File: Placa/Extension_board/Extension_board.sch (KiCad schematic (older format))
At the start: 4 parts

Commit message: Finalizacion del esquematico y creacion del layout
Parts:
- removed C?: C, symbol Device:C
- added D1: D_Zener, Diode_SMD:D_0805_2012Metric, symbol Device:D_Zener
- added D2, D3: LED, Diode_SMD:D_0805_2012Metric, symbol Device:LED
- added J3: Conn_01x04_Male, Connector_PinHeader_1.27mm:PinHeader_1x04_P1.27mm_Vertical, symbol Connector:Conn_01x04_Male
- added R1, R2, R3: 1Ω, Resistor_SMD:R_0805_2012Metric, symbol Device:R
- added R4, R5: 1kΩ, Resistor_SMD:R_0805_2012Metric, symbol Device:R
- J1: renamed from J?; footprint (none) -> Connector_PinHeader_1.27mm:PinHeader_1x05_P1.27mm_Vertical
- J2: renamed from J?; footprint (none) -> Connector_USB:USB_Micro-B_Wuerth_629105150521
- U1: renamed from U?; footprint XDCR_STEVAL-STLCS01V1 -> STEVAL-STLCS01V1_footprint:XDCR_STEVAL-STLCS01V1
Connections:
- net labels added: VIN
- net labels removed: 3.3V, MIC_CLK, SD_CS, SD_MISO, SD_MOSI, SD_SCK
- wire segments 16 -> 24
- no-connect marks 2 -> 10
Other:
- note added: "N3-I2C"
- note added: "N4-Regulación"
- note added: "N5-LEDs"
- note added: "N6-STEVAL-STLCR01V1"
- note added: "Rpz=(Vs-Vz)/((Iz*1.1)+Il)\nRpz=(5v-4.7v)/(53mA*1.1+100mA)\nRpz=2,84Ω"
- note removed: "Dudas:\nD1: La disposicion de los pines del simbolo Micro USB,\n no son identicas al estipulado en el pdf del fabricante, \npor ende se opto por usar estas ultimas disposiciones. \nComprobar si son correctas."
- note removed: "N3-STEVAL-STLCR01V1"
- moved on the sheet: J2, U1

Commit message: Version 2.1 del proyecto
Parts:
- removed D3: LED, Diode_SMD:D_0805_2012Metric, symbol Device:LED
- removed J1: Conn_01x05_Male, Connector_PinHeader_1.27mm:PinHeader_1x05_P1.27mm_Vertical, symbol Connector:Conn_01x05_Male
- removed R2, R3: 1Ω, Resistor_SMD:R_0805_2012Metric, symbol Device:R
- removed R5: 1kΩ, Resistor_SMD:R_0805_2012Metric, symbol Device:R
- added J1: USB_B_Micro, Connector_USB:USB_Micro-B_Wuerth_629105150521, symbol Connector:USB_B_Micro
- J3: footprint Connector_PinHeader_1.27mm:PinHeader_1x04_P1.27mm_Vertical -> Connector_PinHeader_1.00mm:PinHeader_1x04_P1.00mm_Vertical_SMD_Pin1Left
- R1: value 1Ω -> 1,2Ω
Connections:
- net GND: now also J1.5 (GND)
- net RESET: now also J1.3 (D+)
- net SWDCLK: now also J1.2 (D-)
- net SWDIO: now also J1.1 (VBUS)
- net VIN: now also J3.1 (Pin_1), R1.1
- net V_USB: no longer J3.1 (Pin_1)
- no-connect marks 10 -> 11
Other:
- note added: "Rpz=(Vs-Vz)/((Iz*1.1)+Il+Ii2c)\nRpz=(5v-3.3v)/(53mA*1.1+100mA+150mA)\nRpz=1.2Ω"
- note removed: "Rpz=(Vs-Vz)/((Iz*1.1)+Il)\nRpz=(5v-4.7v)/(53mA*1.1+100mA)\nRpz=2,84Ω"
- moved on the sheet: D1, D2, R1, R4
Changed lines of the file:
@@
 Text Notes 1000 1050 0    50   ~ 0
 N1-Entrada_de_voltaje
-$Comp
-L Connector:Conn_01x05_Male J1
-U 1 1 60BBD811
-P 1350 3100
-F 0 "J1" H 1458 3481 50  0000 C CNN
-F 1 "Conn_01x05_Male" H 1458 3390 50  0000 C CNN
-F 2 "Connector_PinHeader_1.27mm:PinHeader_1x05_P1.27mm_Vertical" H 1350 3100 50  0001 C CNN
-F 3 "~" H 1350 3100 50  0001 C CNN
-	1    1350 3100
-	1    0    0    -1
-$EndComp
-Wire Wire Line
-	1550 3000 1850 3000
-Wire Wire Line
-	1550 3100 1850 3100
-Wire Wire Line
-	1550 3200 1850 3200
-Wire Wire Line
-	1550 3300 1850 3300
-Wire Wire Line
-	1550 2900 1850 2900
-NoConn ~ 1850 2900
-Text Label 1850 3000 0    50   ~ 0
+Text Label 1800 3300 0    50   ~ 0
 SWDCLK
-Text Label 1850 3100 0    50   ~ 0
-GND
-Text Label 1850 3200 0    50   ~ 0
+Text Label 1800 3400 0    50   ~ 0
+GND
+Text Label 1800 3100 0    50   ~ 0
 SWDIO
-Text Label 1850 3300 0    50   ~ 0
+Text Label 1800 3200 0    50   ~ 0
 RESET
-Wire Notes Line
-	1000 2650 1000 3500
-Wire Notes Line
-	1000 3500 2200 3500
-Wire Notes Line
-	2200 3500 2200 2650
 Wire Notes Line
 	2200 2650 1000 2650
@@
 L Device:D_Zener D1
 U 1 1 60BFFB26
-P 2450 4400
-F 0 "D1" V 2404 4480 50  0000 L CNN
-F 1 "D_Zener" V 2495 4480 50  0000 L CNN
-F 2 "Diode_SMD:D_0805_2012Metric" H 2450 4400 50  0001 C CNN
-F 3 "~" H 2450 4400 50  0001 C CNN
-	1    2450 4400
+P 2400 4650
+F 0 "D1" V 2354 4730 50  0000 L CNN
+F 1 "D_Zener" V 2445 4730 50  0000 L CNN
+F 2 "Diode_SMD:D_0805_2012Metric" H 2400 4650 50  0001 C CNN
+F 3 "~" H 2400 4650 50  0001 C CNN
+	1    2400 4650
 	0    1    1    0
 $EndComp
-Text Label 1250 4050 2    50   ~ 0
+Text Label 1200 4300 2    50   ~ 0
 V_USB
-Text Label 1200 4550 2    50   ~ 0
-GND
-Text Label 2600 4050 0    50   ~ 0
+Text Label 1150 4800 2    50   ~ 0
+GND
+Text Label 2550 4300 0    50   ~ 0
 VIN
 $Comp
 L Device:R R1
 U 1 1 60C00A3D
-P 1400 4050
-F 0 "R1" V 1193 4050 50  0000 C CNN
-F 1 "1Ω" V 1284 4050 50  0000 C CNN
-F 2 "Resistor_SMD:R_0805_2012Metric" V 1330 4050 50  0001 C CNN
-F 3 "~" H 1400 4050 50  0001 C CNN
-	1    1400 4050
+P 1850 4300
+F 0 "R1" V 1643 4300 50  0000 C CNN
+F 1 "1,2Ω" V 1734 4300 50  0000 C CNN
+F 2 "Resistor_SMD:R_0805_2012Metric" V 1780 4300 50  0001 C CNN
+F 3 "~" H 1850 4300 50  0001 C CNN
+	1    1850 4300
 	0    1    1    0
 $EndComp
-Text Notes 1000 3700 0    50   ~ 0
+Text Notes 950  3950 0    50   ~ 0
 N4-Regulación
 NoConn ~ 4250 2250
@@
 Text Notes 2350 2600 0    50   ~ 0
 N3-I2C
-$Comp
-L Device:R R2
-U 1 1 60C21078
-P 1800 4050
-F 0 "R2" V 2007 4050 50  0000 C CNN
-F 1 "1Ω" V 1916 4050 50  0000 C CNN
-F 2 "Resistor_SMD:R_0805_2012Metric" V 1730 4050 50  0001 C CNN
-F 3 "~" H 1800 4050 50  0001 C CNN
-	1    1800 4050
-	0    -1   -1   0
-$EndComp
-$Comp
-L Device:R R3
-U 1 1 60C2144B
-P 2200 4050
-F 0 "R3" V 2407 4050 50  0000 C CNN
-F 1 "1Ω" V 2316 4050 50  0000 C CNN
-F 2 "Resistor_SMD:R_0805_2012Metric" V 2130 4050 50  0001 C CNN
-F 3 "~" H 2200 4050 50  0001 C CNN
-	1    2200 4050
-	0    -1   -1   0
-$EndComp
-Wire Wire Line
-	1550 4050 1650 4050
-Wire Wire Line
-	1950 4050 2050 4050
-Wire Wire Line
-	1200 4550 2450 4550
-Wire Wire Line
-	2450 4250 2450 4050
-Wire Wire Line
-	2450 4050 2350 4050
-Wire Wire Line
-	2450 4050 2600 4050
-Connection ~ 2450 4050
-Wire Notes Line
-	1000 3750 1000 4600
-Wire Notes Line
-	1000 4600 2850 4600
-Wire Notes Line
-	2850 4600 2850 3750
-Wire Notes Line
-	1000 3750 2850 3750
-Text Label 3100 2900 0    50   ~ 0
-V_USB
+Wire Wire Line
+	1150 4800 2400 4800
+Wire Wire Line
+	2400 4500 2400 4300
+Wire Wire Line
+	2400 4300 2550 4300
+Wire Notes Line
+	950  4000 950  4850
+Wire Notes Line
+	950  4850 2800 4850
+Wire Notes Line
+	2800 4850 2800 4000
+Wire Notes Line
+	950  4000 2800 4000
 Text Label 3100 3200 0    50   ~ 0
 GND
@@
 F 0 "J3" H 2708 3281 50  0000 C CNN
 F 1 "Conn_01x04_Male" H 2708 3190 50  0000 C CNN
-F 2 "Connector_PinHeader_1.27mm:PinHeader_1x04_P1.27mm_Vertical" H 2600 3000 50  0001 C CNN
+F 2 "Connector_PinHeader_1.00mm:PinHeader_1x04_P1.00mm_Vertical_SMD_Pin1Left" H 2600 3000 50  0001 C CNN
 F 3 "~" H 2600 3000 50  0001 C CNN
 	1    2600 3000
@@
 Wire Wire Line
 	1650 2200 2300 2200
-Text Notes 3000 4300 0    59   ~ 0
-Rpz=(Vs-Vz)/((Iz*1.1)+Il)\nRpz=(5v-4.7v)/(53mA*1.1+100mA)\nRpz=2,84Ω
+Text Notes 2950 4550 0    59   ~ 0
+Rpz=(Vs-Vz)/((Iz*1.1)+Il+Ii2c)\nRpz=(5v-3.3v)/(53mA*1.1+100mA+150mA)\nRpz=1.2Ω
 $Comp
 L Device:LED D2
 U 1 1 60C6CD3B
-P 2050 5150
-F 0 "D2" H 2043 4895 50  0000 C CNN
-F 1 "LED" H 2043 4986 50  0000 C CNN
-F 2 "Diode_SMD:D_0805_2012Metric" H 2050 5150 50  0001 C CNN
-F 3 "~" H 2050 5150 50  0001 C CNN
-	1    2050 5150
-	-1   0    0    1
-$EndComp
-$Comp
-L Device:LED D3
-U 1 1 60C6DA9C
-P 2050 5500
-F 0 "D3" H 2043 5245 50  0000 C CNN
-F 1 "LED" H 2043 5336 50  0000 C CNN
-F 2 "Diode_SMD:D_0805_2012Metric" H 2050 5500 50  0001 C CNN
-F 3 "~" H 2050 5500 50  0001 C CNN
-	1    2050 5500
+P 2000 5400
+F 0 "D2" H 1993 5145 50  0000 C CNN
+F 1 "LED" H 1993 5236 50  0000 C CNN
+F 2 "Diode_SMD:D_0805_2012Metric" H 2000 5400 50  0001 C CNN
+F 3 "~" H 2000 5400 50  0001 C CNN
+	1    2000 5400
 	-1   0    0    1
 $EndComp
@@
 L Device:R R4
 U 1 1 60C6E1B1
-P 1500 5150
-F 0 "R4" V 1293 5150 50  0000 C CNN
-F 1 "1kΩ" V 1384 5150 50  0000 C CNN
-F 2 "Resistor_SMD:R_0805_2012Metric" V 1430 5150 50  0001 C CNN
-F 3 "~" H 1500 5150 50  0001 C CNN
-	1    1500 5150
+P 1450 5400
+F 0 "R4" V 1243 5400 50  0000 C CNN
+F 1 "1kΩ" V 1334 5400 50  0000 C CNN
+F 2 "Resistor_SMD:R_0805_2012Metric" V 1380 5400 50  0001 C CNN
+F 3 "~" H 1450 5400 50  0001 C CNN
+	1    1450 5400
 	0    1    1    0
 $EndComp
-$Comp
-L Device:R R5
-U 1 1 60C6E5D7
-P 1500 5500
-F 0 "R5" V 1293 5500 50  0000 C CNN
-F 1 "1kΩ" V 1384 5500 50  0000 C CNN
-F 2 "Resistor_SMD:R_0805_2012Metric" V 1430 5500 50  0001 C CNN
-F 3 "~" H 1500 5500 50  0001 C CNN
-	1    1500 5500
-	0    1    1    0
-$EndComp
-Text Label 2450 5150 0    50   ~ 0
-GND
-Text Label 2450 5500 0    50   ~ 0
-GND
-Wire Wire Line
-	2200 5500 2450 5500
-Wire Wire Line
-	2200 5150 2450 5150
-Wire Wire Line
-	1650 5150 1900 5150
-Wire Wire Line
-	1650 5500 1900 5500
-Text Label 1350 5150 2    50   ~ 0
+Text Label 2400 5400 0    50   ~ 0
+GND
+Wire Wire Line
+	2150 5400 2400 5400
+Wire Wire Line
+	1600 5400 1850 5400
+Text Label 1300 5400 2    50   ~ 0
 V_USB
-Text Label 1350 5500 2    50   ~ 0
-SWDCLK
-Wire Notes Line
-	1000 4850 1000 5600
-Wire Notes Line
-	1000 5600 2650 5600
-Wire Notes Line
-	2650 5600 2650 4850
-Wire Notes Line
-	2650 4850 1000 4850
-Text Notes 1050 4800 0    50   ~ 0
+Wire Notes Line
+	2600 5100 950  5100
+Text Notes 1000 5050 0    50   ~ 0
 N5-LEDs
+$Comp
+L Connector:USB_B_Micro J1
+U 1 1 60C7DFF7
+P 1300 3200
+F 0 "J1" H 1357 3667 50  0000 C CNN
+F 1 "USB_B_Micro" H 1357 3576 50  0000 C CNN
+F 2 "Connector_USB:USB_Micro-B_Wuerth_629105150521" H 1450 3150 50  0001 C CNN
+F 3 "~" H 1450 3150 50  0001 C CNN
+	1    1300 3200
+	1    0    0    -1
+$EndComp
+Wire Notes Line
+	950  5100 950  5500
+Wire Notes Line
+	950  5500 2600 5500
+Wire Notes Line
+	2600 5500 2600 5100
+Wire Wire Line
+	1600 3000 1800 3000
+Wire Wire Line
+	1800 3000 1800 3100
+Wire Wire Line
+	1600 3200 1800 3200
+Wire Wire Line
+	1600 3300 1800 3300
+Wire Wire Line
+	1300 3600 1800 3600
+Wire Wire Line
+	1800 3600 1800 3400
+NoConn ~ 1600 3400
+NoConn ~ 1200 3600
+Wire Notes Line
+	1000 3650 2200 3650
+Wire Notes Line
+	1000 2650 1000 3650
+Wire Notes Line
+	2200 2650 2200 3650
+Wire Wire Line
+	2000 4300 2400 4300
+Connection ~ 2400 4300
+Wire Wire Line
+	1200 4300 1700 4300
+Text Label 3100 2900 0    50   ~ 0
+VIN
 $EndSCHEMATC

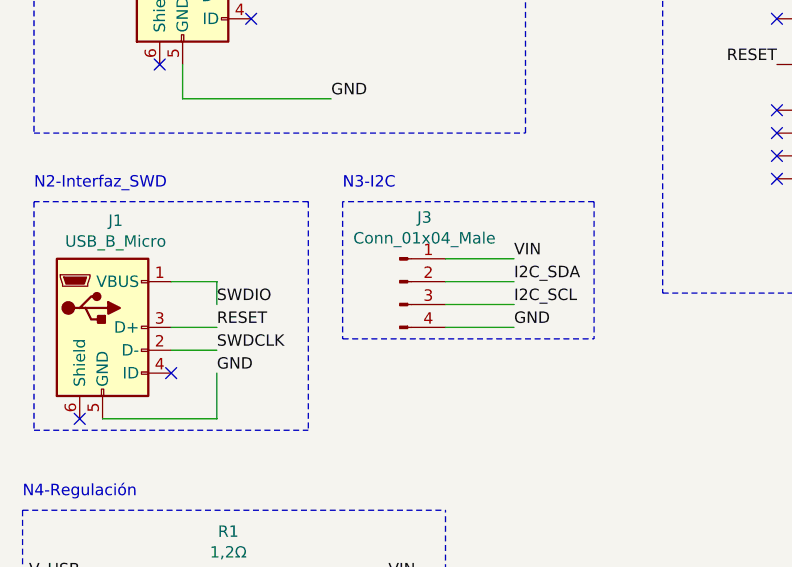
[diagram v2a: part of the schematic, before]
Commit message: Cambio de ubicacion, componentes y footprints
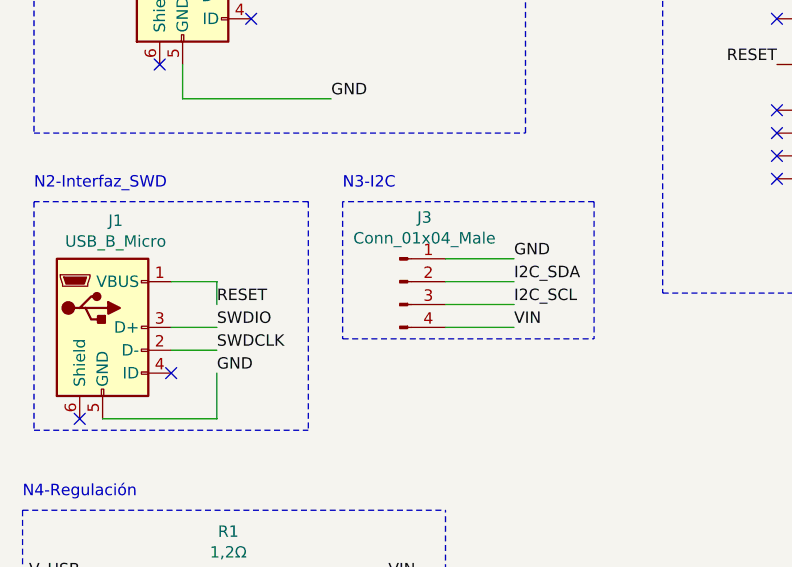
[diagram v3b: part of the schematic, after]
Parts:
- D1, D2: footprint Diode_SMD:D_0805_2012Metric -> Resistor_THT:R_Axial_DIN0204_L3.6mm_D1.6mm_P1.90mm_Vertical
- J3: footprint Connector_PinHeader_1.00mm:PinHeader_1x04_P1.00mm_Vertical_SMD_Pin1Left -> Connector_PinHeader_2.54mm:PinHeader_1x04_P2.54mm_Horizontal
- R1, R4: footprint Resistor_SMD:R_0805_2012Metric -> Resistor_THT:R_Axial_DIN0204_L3.6mm_D1.6mm_P1.90mm_Vertical
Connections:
- net GND: now also J3.1 (Pin_1); no longer J3.4 (Pin_4)
- net RESET: now also J1.1 (VBUS); no longer J1.3 (D+)
- net SWDIO: now also J1.3 (D+); no longer J1.1 (VBUS)
- net VIN: now also J3.4 (Pin_4); no longer J3.1 (Pin_1)
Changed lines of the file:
@@
 Text Label 1800 3400 0    50   ~ 0
 GND
+Text Label 1800 3200 0    50   ~ 0
+SWDIO
 Text Label 1800 3100 0    50   ~ 0
-SWDIO
-Text Label 1800 3200 0    50   ~ 0
 RESET
 Wire Notes Line
@@
 F 0 "D1" V 2354 4730 50  0000 L CNN
 F 1 "D_Zener" V 2445 4730 50  0000 L CNN
-F 2 "Diode_SMD:D_0805_2012Metric" H 2400 4650 50  0001 C CNN
+F 2 "Resistor_THT:R_Axial_DIN0204_L3.6mm_D1.6mm_P1.90mm_Vertical" H 2400 4650 50  0001 C CNN
 F 3 "~" H 2400 4650 50  0001 C CNN
 	1    2400 4650
@@
 F 0 "R1" V 1643 4300 50  0000 C CNN
 F 1 "1,2Ω" V 1734 4300 50  0000 C CNN
-F 2 "Resistor_SMD:R_0805_2012Metric" V 1780 4300 50  0001 C CNN
+F 2 "Resistor_THT:R_Axial_DIN0204_L3.6mm_D1.6mm_P1.90mm_Vertical" V 1780 4300 50  0001 C CNN
 F 3 "~" H 1850 4300 50  0001 C CNN
 	1    1850 4300
@@
 Wire Notes Line
 	950  4000 2800 4000
-Text Label 3100 3200 0    50   ~ 0
+Text Label 3100 2900 0    50   ~ 0
 GND
 $Comp
@@
 F 0 "J3" H 2708 3281 50  0000 C CNN
 F 1 "Conn_01x04_Male" H 2708 3190 50  0000 C CNN
-F 2 "Connector_PinHeader_1.00mm:PinHeader_1x04_P1.00mm_Vertical_SMD_Pin1Left" H 2600 3000 50  0001 C CNN
+F 2 "Connector_PinHeader_2.54mm:PinHeader_1x04_P2.54mm_Horizontal" H 2600 3000 50  0001 C CNN
 F 3 "~" H 2600 3000 50  0001 C CNN
 	1    2600 3000
@@
 F 0 "D2" H 1993 5145 50  0000 C CNN
 F 1 "LED" H 1993 5236 50  0000 C CNN
-F 2 "Diode_SMD:D_0805_2012Metric" H 2000 5400 50  0001 C CNN
+F 2 "Resistor_THT:R_Axial_DIN0204_L3.6mm_D1.6mm_P1.90mm_Vertical" H 2000 5400 50  0001 C CNN
 F 3 "~" H 2000 5400 50  0001 C CNN
 	1    2000 5400
@@
 F 0 "R4" V 1243 5400 50  0000 C CNN
 F 1 "1kΩ" V 1334 5400 50  0000 C CNN
-F 2 "Resistor_SMD:R_0805_2012Metric" V 1380 5400 50  0001 C CNN
+F 2 "Resistor_THT:R_Axial_DIN0204_L3.6mm_D1.6mm_P1.90mm_Vertical" V 1380 5400 50  0001 C CNN
 F 3 "~" H 1450 5400 50  0001 C CNN
 	1    1450 5400
@@
 Wire Wire Line
 	1200 4300 1700 4300
-Text Label 3100 2900 0    50   ~ 0
+Text Label 3100 3200 0    50   ~ 0
 VIN
 $EndSCHEMATC

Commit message: Cambio de footprint usb
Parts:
- J1, J2: footprint Connector_USB:USB_Micro-B_Wuerth_629105150521 -> freetronics_footprints:USB-MICRO-5pin_PTHMOUNT
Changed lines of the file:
@@
 F 0 "J2" H 1707 2117 50  0000 C CNN
 F 1 "USB_B_Micro" H 1707 2026 50  0000 C CNN
-F 2 "Connector_USB:USB_Micro-B_Wuerth_629105150521" H 1800 1600 50  0001 C CNN
+F 2 "freetronics_footprints:USB-MICRO-5pin_PTHMOUNT" H 1800 1600 50  0001 C CNN
 F 3 "~" H 1800 1600 50  0001 C CNN
 	1    1650 1650
@@
 F 0 "J1" H 1357 3667 50  0000 C CNN
 F 1 "USB_B_Micro" H 1357 3576 50  0000 C CNN
-F 2 "Connector_USB:USB_Micro-B_Wuerth_629105150521" H 1450 3150 50  0001 C CNN
+F 2 "freetronics_footprints:USB-MICRO-5pin_PTHMOUNT" H 1450 3150 50  0001 C CNN
 F 3 "~" H 1450 3150 50  0001 C CNN
 	1    1300 3200

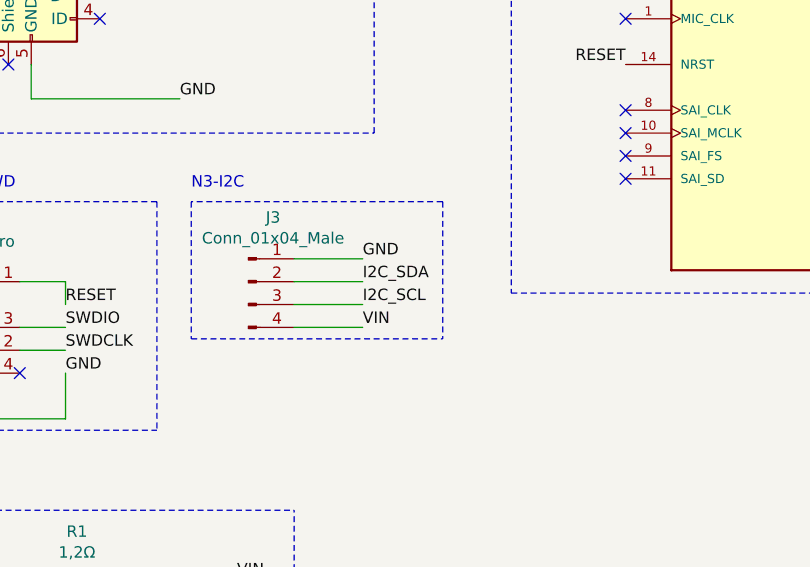
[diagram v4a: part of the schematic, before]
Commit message: Ampliacion de los pads de los componentes
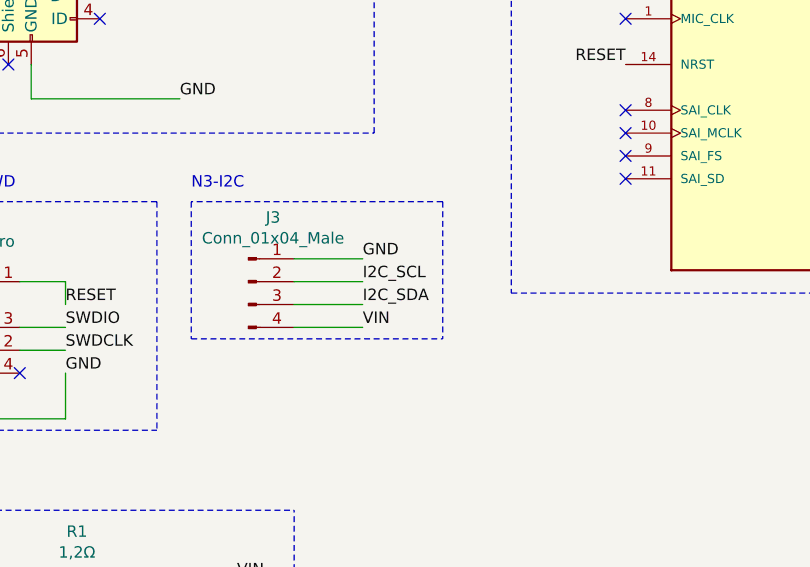
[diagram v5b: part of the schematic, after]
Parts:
- D1: footprint Resistor_THT:R_Axial_DIN0204_L3.6mm_D1.6mm_P1.90mm_Vertical -> Resistor_THT:R_Axial_DIN0207_L6.3mm_D2.5mm_P5.08mm_Vertical
- D2: footprint Resistor_THT:R_Axial_DIN0204_L3.6mm_D1.6mm_P1.90mm_Vertical -> LED_THT:LED_D5.0mm_IRBlack
- R1, R4: footprint Resistor_THT:R_Axial_DIN0204_L3.6mm_D1.6mm_P1.90mm_Vertical -> Resistor_THT:R_Axial_DIN0207_L6.3mm_D2.5mm_P7.62mm_Horizontal
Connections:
- net I2C_SCL: now also J3.2 (Pin_2); no longer J3.3 (Pin_3)
- net I2C_SDA: now also J3.3 (Pin_3); no longer J3.2 (Pin_2)
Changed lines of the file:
@@
 F 0 "D1" V 2354 4730 50  0000 L CNN
 F 1 "D_Zener" V 2445 4730 50  0000 L CNN
-F 2 "Resistor_THT:R_Axial_DIN0204_L3.6mm_D1.6mm_P1.90mm_Vertical" H 2400 4650 50  0001 C CNN
+F 2 "Resistor_THT:R_Axial_DIN0207_L6.3mm_D2.5mm_P5.08mm_Vertical" H 2400 4650 50  0001 C CNN
 F 3 "~" H 2400 4650 50  0001 C CNN
 	1    2400 4650
@@
 F 0 "R1" V 1643 4300 50  0000 C CNN
 F 1 "1,2Ω" V 1734 4300 50  0000 C CNN
-F 2 "Resistor_THT:R_Axial_DIN0204_L3.6mm_D1.6mm_P1.90mm_Vertical" V 1780 4300 50  0001 C CNN
+F 2 "Resistor_THT:R_Axial_DIN0207_L6.3mm_D2.5mm_P7.62mm_Horizontal" V 1780 4300 50  0001 C CNN
 F 3 "~" H 1850 4300 50  0001 C CNN
 	1    1850 4300
@@
 NoConn ~ 4250 2550
 NoConn ~ 6050 1450
+Text Label 3100 3100 0    50   ~ 0
+I2C_SDA
 Text Label 3100 3000 0    50   ~ 0
-I2C_SDA
-Text Label 3100 3100 0    50   ~ 0
 I2C_SCL
 Wire Notes Line
@@
 F 0 "D2" H 1993 5145 50  0000 C CNN
 F 1 "LED" H 1993 5236 50  0000 C CNN
-F 2 "Resistor_THT:R_Axial_DIN0204_L3.6mm_D1.6mm_P1.90mm_Vertical" H 2000 5400 50  0001 C CNN
+F 2 "LED_THT:LED_D5.0mm_IRBlack" H 2000 5400 50  0001 C CNN
 F 3 "~" H 2000 5400 50  0001 C CNN
 	1    2000 5400
@@
 F 0 "R4" V 1243 5400 50  0000 C CNN
 F 1 "1kΩ" V 1334 5400 50  0000 C CNN
-F 2 "Resistor_THT:R_Axial_DIN0204_L3.6mm_D1.6mm_P1.90mm_Vertical" V 1380 5400 50  0001 C CNN
+F 2 "Resistor_THT:R_Axial_DIN0207_L6.3mm_D2.5mm_P7.62mm_Horizontal" V 1380 5400 50  0001 C CNN
 F 3 "~" H 1450 5400 50  0001 C CNN
 	1    1450 5400
